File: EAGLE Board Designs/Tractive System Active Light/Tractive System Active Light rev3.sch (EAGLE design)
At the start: 31 parts, among them X2 MAIN

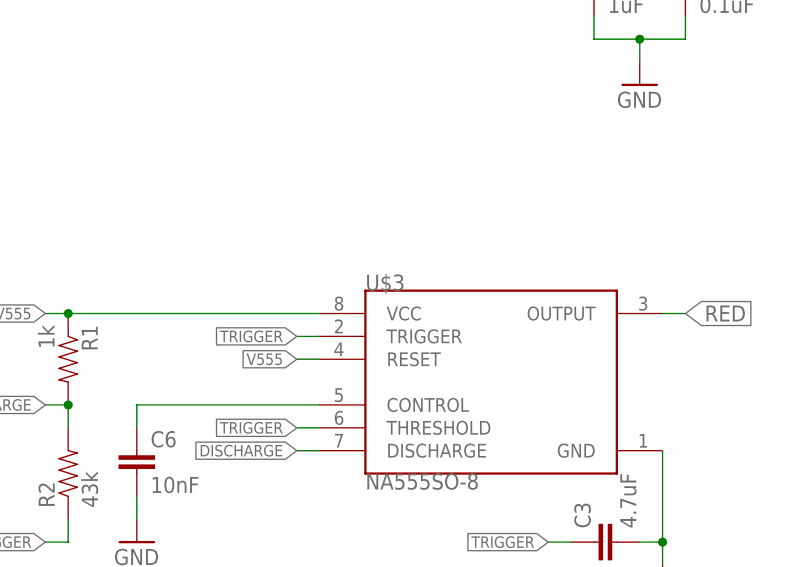
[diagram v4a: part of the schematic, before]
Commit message: Changes in board review
This reverts commit d30a44cf333b6e75a81830c5357fabca05badc4e.
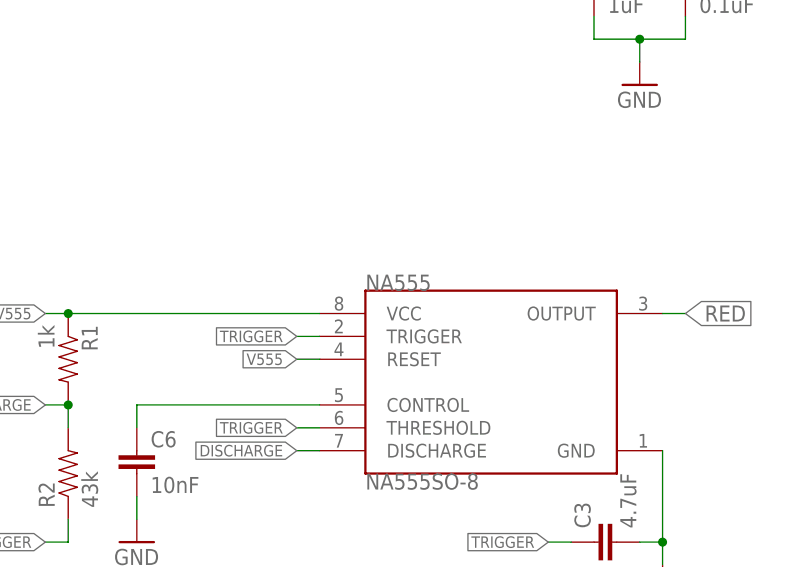
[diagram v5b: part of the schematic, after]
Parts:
- renumbered U$3 to NA555
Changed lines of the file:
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@@
 <part name="D2" library="HyTechDevices" deviceset="DIODE_ZENER" device="" value="MMBZ5246BLT1G"/>
 <part name="D1" library="HyTechDevices" deviceset="DIODE_ZENER" device="" value="MMBZ5246BLT1G"/>
-<part name="U$3" library="HyTechDevices" deviceset="NA555" device="SO-8"/>
+<part name="NA555" library="HyTechDevices" deviceset="NA555" device="SO-8"/>
 <part name="R8" library="HyTechDevices" deviceset="RESISTOR" device="0603-RES" value="10">
 <attribute name="TOLERANCE" value="1%"/>
@@
 <attribute name="NAME" x="85.09" y="-34.7726" size="1.778" layer="95" rot="R180"/>
 </instance>
-<instance part="U$3" gate="G$1" x="25.4" y="2.54" smashed="yes">
+<instance part="NA555" gate="G$1" x="25.4" y="2.54" smashed="yes">
 <attribute name="NAME" x="25.4" y="22.86" size="1.778" layer="95"/>
 <attribute name="VALUE" x="25.4" y="2.54" size="1.778" layer="96" align="top-left"/>
@@
 <wire x1="0" y1="7.62" x2="0" y2="10.16" width="0.1524" layer="91"/>
 <pinref part="C6" gate="G$1" pin="1"/>
-<pinref part="U$3" gate="G$1" pin="CONTROL"/>
+<pinref part="NA555" gate="G$1" pin="CONTROL"/>
 <wire x1="0" y1="10.16" x2="20.32" y2="10.16" width="0.1524" layer="91"/>
 </segment>
@@
 <wire x1="55.88" y1="-5.08" x2="58.42" y2="-5.08" width="0.1524" layer="91"/>
 <junction x="58.42" y="-5.08"/>
-<pinref part="U$3" gate="G$1" pin="GND"/>
+<pinref part="NA555" gate="G$1" pin="GND"/>
 </segment>
 <segment>
@@
 </segment>
 <segment>
-<pinref part="U$3" gate="G$1" pin="RESET"/>
+<pinref part="NA555" gate="G$1" pin="RESET"/>
 <wire x1="20.32" y1="15.24" x2="17.78" y2="15.24" width="0.1524" layer="91"/>
 <label x="17.78" y="15.24" size="1.27" layer="95" font="vector" rot="R180" xref="yes"/>
 </segment>
 <segment>
-<pinref part="U$3" gate="G$1" pin="VCC"/>
+<pinref part="NA555" gate="G$1" pin="VCC"/>
 <pinref part="R1" gate="G$1" pin="1"/>
 <wire x1="-7.62" y1="20.32" x2="20.32" y2="20.32" width="0.1524" layer="91"/>
@@
 <wire x1="58.42" y1="20.32" x2="60.96" y2="20.32" width="0.1524" layer="91"/>
 <label x="60.96" y="20.32" size="1.778" layer="95" xref="yes"/>
-<pinref part="U$3" gate="G$1" pin="OUTPUT"/>
+<pinref part="NA555" gate="G$1" pin="OUTPUT"/>
 </segment>
 <segment>
@@
 </segment>
 <segment>
-<pinref part="U$3" gate="G$1" pin="TRIGGER"/>
+<pinref part="NA555" gate="G$1" pin="TRIGGER"/>
 <wire x1="20.32" y1="17.78" x2="17.78" y2="17.78" width="0.1524" layer="91"/>
 <label x="17.78" y="17.78" size="1.27" layer="95" font="vector" rot="R180" xref="yes"/>
 </segment>
 <segment>
-<pinref part="U$3" gate="G$1" pin="THRESHOLD"/>
+<pinref part="NA555" gate="G$1" pin="THRESHOLD"/>
 <wire x1="20.32" y1="7.62" x2="17.78" y2="7.62" width="0.1524" layer="91"/>
 <label x="17.78" y="7.62" size="1.27" layer="95" font="vector" rot="R180" xref="yes"/>
@@
 <net name="DISCHARGE" class="0">
 <segment>
-<pinref part="U$3" gate="G$1" pin="DISCHARGE"/>
+<pinref part="NA555" gate="G$1" pin="DISCHARGE"/>
 <wire x1="20.32" y1="5.08" x2="17.78" y2="5.08" width="0.1524" layer="91"/>
 <label x="17.78" y="5.08" size="1.27" layer="95" font="vector" rot="R180" xref="yes"/>

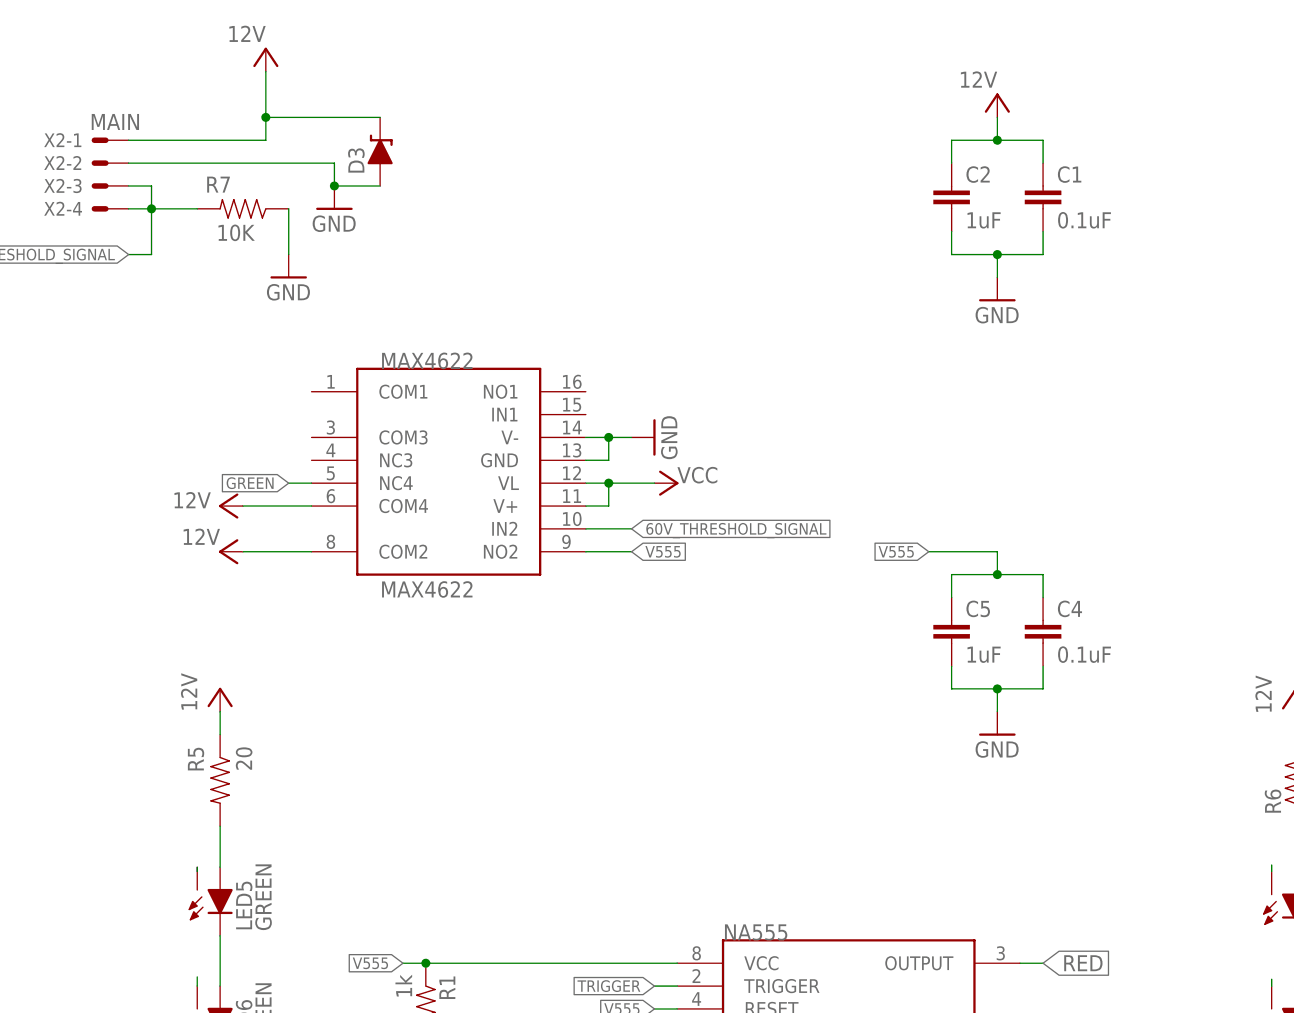
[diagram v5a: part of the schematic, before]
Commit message: Simplified switches, More cooling
Replaced MAX4622 with ADG1423
Moved logos and resistors on the right upwards
Expanded thermal copper for LEDs
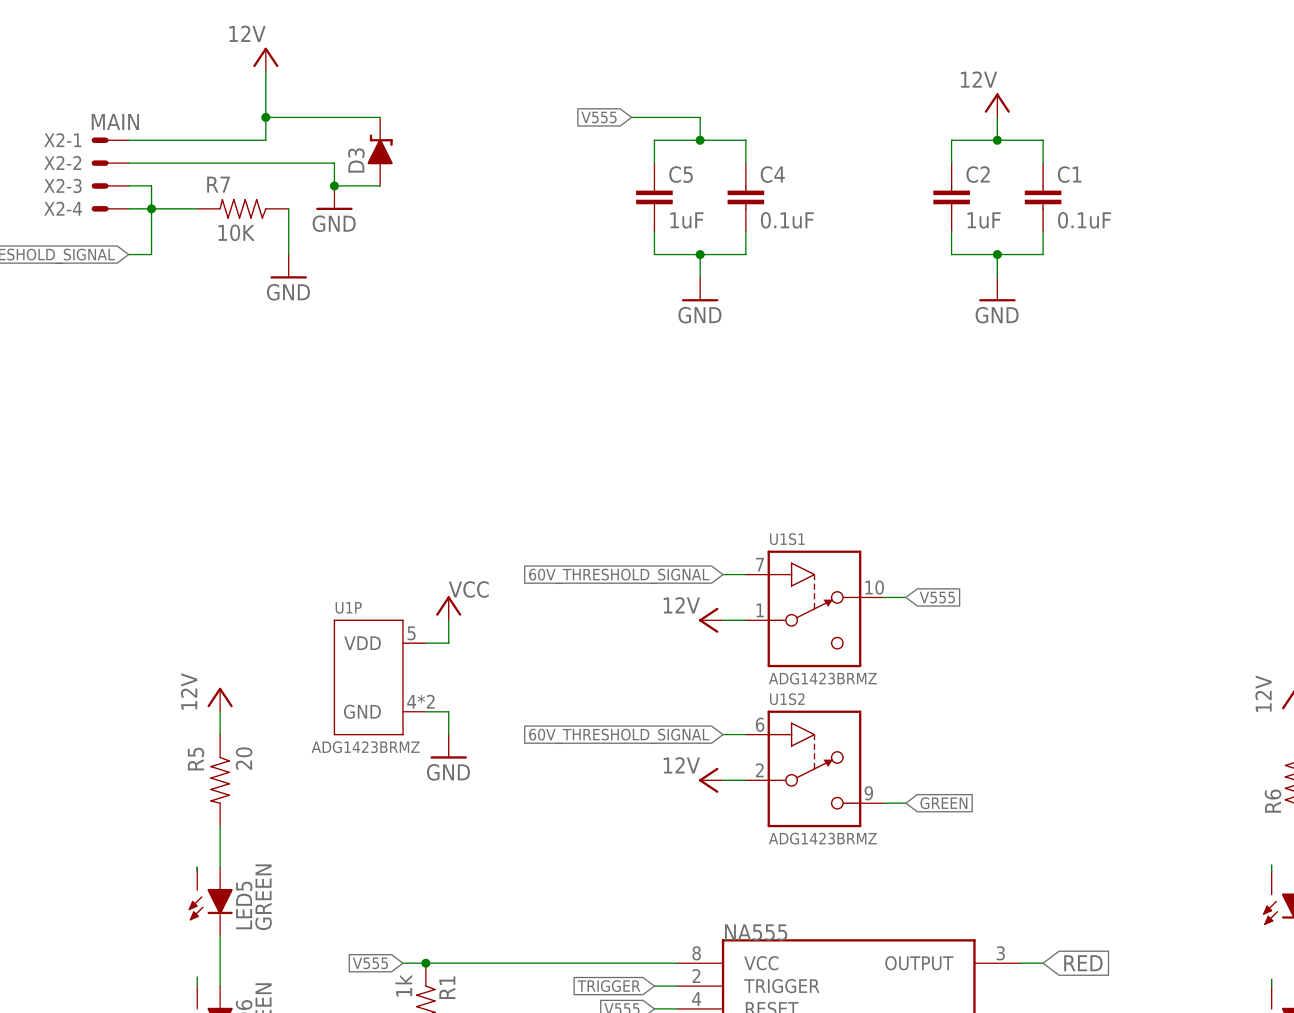
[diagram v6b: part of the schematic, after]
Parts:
- removed MAX4622: MAX4622, HyTechDevices:MAX4622
- added U1: ADG1423, HyTechDevices:ADG1423
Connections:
- net 60V_THRESHOLD_SIGNAL: now also U1S1.IN, U1S2.IN; no longer MAX4622.IN2
- net GND: now also U1P.GND; no longer MAX4622.GND, MAX4622.V-
- net GREEN: now also U1S2.D; no longer MAX4622.NC4
- net V555: now also U1S1.D; no longer MAX4622.NO2
- net VCC: now also U1P.VDD, U1S1.S, U1S2.S; no longer MAX4622.COM2, MAX4622.COM4, MAX4622.V+, MAX4622.VL
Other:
- moved on the sheet: C4, C5

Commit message: Done
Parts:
- renumbered NA555 to U2
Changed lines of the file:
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@@
 <part name="D2" library="HyTechDevices" deviceset="DIODE_ZENER" device="" value="MMBZ5246BLT1G"/>
 <part name="D1" library="HyTechDevices" deviceset="DIODE_ZENER" device="" value="MMBZ5246BLT1G"/>
-<part name="NA555" library="HyTechDevices" deviceset="NA555" device="SO-8"/>
+<part name="U2" library="HyTechDevices" deviceset="NA555" device="SO-8"/>
 <part name="R8" library="HyTechDevices" deviceset="RESISTOR" device="0603-RES" value="10">
 <attribute name="TOLERANCE" value="1%"/>
@@
 <attribute name="NAME" x="85.09" y="-34.7726" size="1.778" layer="95" rot="R180"/>
 </instance>
-<instance part="NA555" gate="G$1" x="25.4" y="2.54" smashed="yes">
+<instance part="U2" gate="G$1" x="25.4" y="2.54" smashed="yes">
 <attribute name="NAME" x="25.4" y="22.86" size="1.778" layer="95"/>
 <attribute name="VALUE" x="25.4" y="2.54" size="1.778" layer="96" align="top-left"/>
@@
 <wire x1="0" y1="7.62" x2="0" y2="10.16" width="0.1524" layer="91"/>
 <pinref part="C6" gate="G$1" pin="1"/>
-<pinref part="NA555" gate="G$1" pin="CONTROL"/>
+<pinref part="U2" gate="G$1" pin="CONTROL"/>
 <wire x1="0" y1="10.16" x2="20.32" y2="10.16" width="0.1524" layer="91"/>
 </segment>
@@
 <wire x1="55.88" y1="-5.08" x2="58.42" y2="-5.08" width="0.1524" layer="91"/>
 <junction x="58.42" y="-5.08"/>
-<pinref part="NA555" gate="G$1" pin="GND"/>
+<pinref part="U2" gate="G$1" pin="GND"/>
 </segment>
 <segment>
@@
 </segment>
 <segment>
-<pinref part="NA555" gate="G$1" pin="RESET"/>
+<pinref part="U2" gate="G$1" pin="RESET"/>
 <wire x1="20.32" y1="15.24" x2="17.78" y2="15.24" width="0.1524" layer="91"/>
 <label x="17.78" y="15.24" size="1.27" layer="95" font="vector" rot="R180" xref="yes"/>
 </segment>
 <segment>
-<pinref part="NA555" gate="G$1" pin="VCC"/>
+<pinref part="U2" gate="G$1" pin="VCC"/>
 <pinref part="R1" gate="G$1" pin="1"/>
 <wire x1="-7.62" y1="20.32" x2="20.32" y2="20.32" width="0.1524" layer="91"/>
@@
 <wire x1="58.42" y1="20.32" x2="60.96" y2="20.32" width="0.1524" layer="91"/>
 <label x="60.96" y="20.32" size="1.778" layer="95" xref="yes"/>
-<pinref part="NA555" gate="G$1" pin="OUTPUT"/>
+<pinref part="U2" gate="G$1" pin="OUTPUT"/>
 </segment>
 <segment>
@@
 </segment>
 <segment>
-<pinref part="NA555" gate="G$1" pin="TRIGGER"/>
+<pinref part="U2" gate="G$1" pin="TRIGGER"/>
 <wire x1="20.32" y1="17.78" x2="17.78" y2="17.78" width="0.1524" layer="91"/>
 <label x="17.78" y="17.78" size="1.27" layer="95" font="vector" rot="R180" xref="yes"/>
 </segment>
 <segment>
-<pinref part="NA555" gate="G$1" pin="THRESHOLD"/>
+<pinref part="U2" gate="G$1" pin="THRESHOLD"/>
 <wire x1="20.32" y1="7.62" x2="17.78" y2="7.62" width="0.1524" layer="91"/>
 <label x="17.78" y="7.62" size="1.27" layer="95" font="vector" rot="R180" xref="yes"/>
@@
 <net name="DISCHARGE" class="0">
 <segment>
-<pinref part="NA555" gate="G$1" pin="DISCHARGE"/>
+<pinref part="U2" gate="G$1" pin="DISCHARGE"/>
 <wire x1="20.32" y1="5.08" x2="17.78" y2="5.08" width="0.1524" layer="91"/>
 <label x="17.78" y="5.08" size="1.27" layer="95" font="vector" rot="R180" xref="yes"/>
